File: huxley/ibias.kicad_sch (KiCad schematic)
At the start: 4 parts, among them U2 LM134H

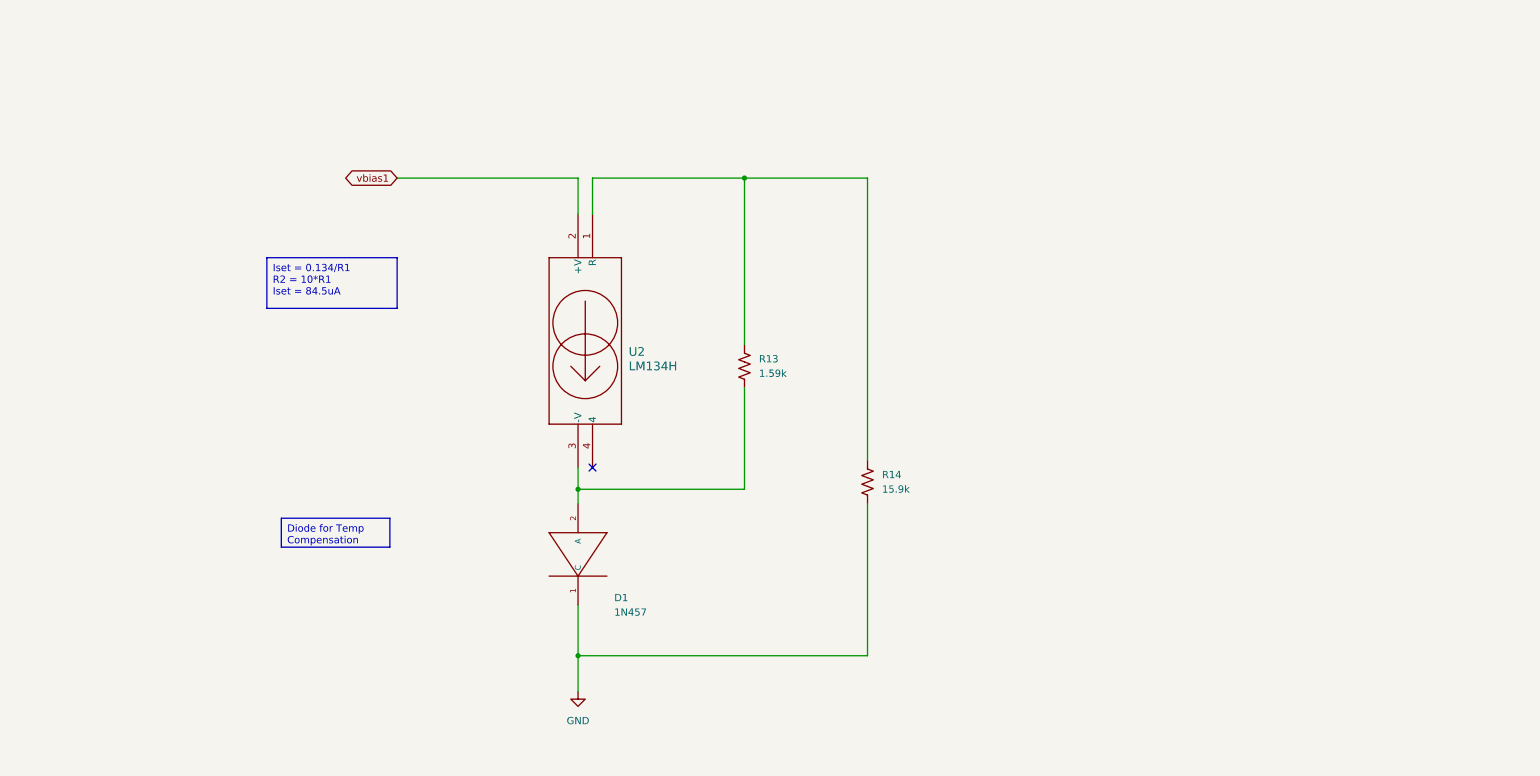
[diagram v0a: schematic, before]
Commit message: updated Ibias gen and footprints
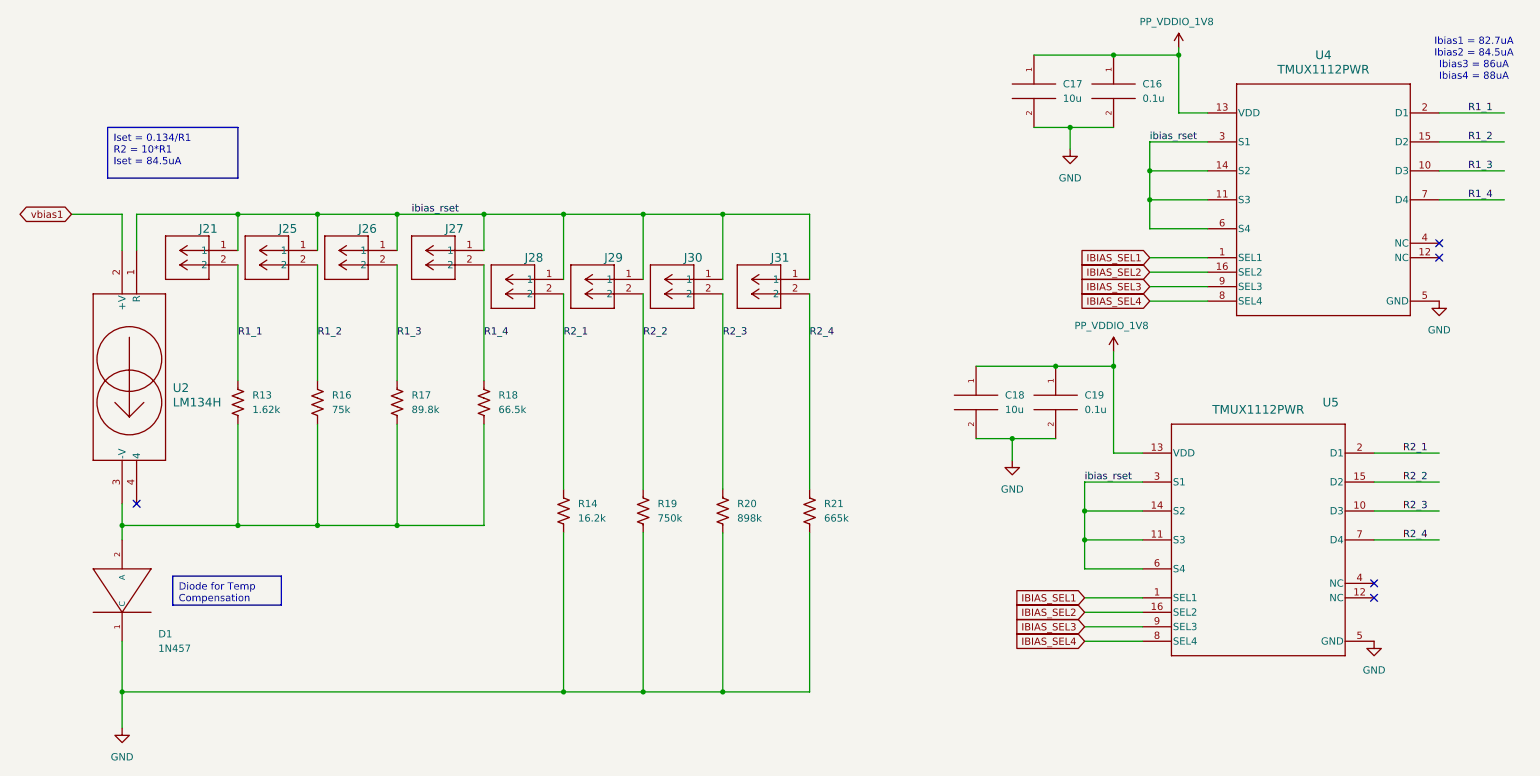
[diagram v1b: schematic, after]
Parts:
- added C16, C19: 0.1u, Capacitor_SMD:C_0402_1005Metric, symbol pspice:C
- added C17, C18: 10u, Capacitor_SMD:C_0402_1005Metric, symbol pspice:C
- added J21, J25, J26, J27, J28, J29, J30, J31: 61300211121, 726_footprints:CONN_61300211121_WRE, symbol _PHASE:61300211121
- added R16: 75k, Resistor_SMD:R_0603_1608Metric, symbol Device:R_US
- added R17: 89.8k, Resistor_SMD:R_0603_1608Metric, symbol Device:R_US
- added R18: 66.5k, Resistor_SMD:R_0603_1608Metric, symbol Device:R_US
- added R19: 750k, Resistor_SMD:R_0603_1608Metric, symbol Device:R_US
- added R20: 898k, Resistor_SMD:R_0603_1608Metric, symbol Device:R_US
- added R21: 665k, Resistor_SMD:R_0603_1608Metric, symbol Device:R_US
- added U4, U5: TMUX1112PWR, 726_footprints:TMUX1111PWR, symbol _PHASE:TMUX1111PWR
- R13: value 1.59k -> 1.62k
- R14: value 15.9k -> 16.2k
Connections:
- net GND: now also C16.2, C17.2, C18.2, C19.2, R19.2, R20.2, R21.2, U4.5 (GND), U5.5 (GND)
- net at D1.2 (A), R13.2, U2.3 (-V): now also R16.2, R17.2, R18.2
- new net IBIAS_SEL1: U4.1 (SEL1), U5.1 (SEL1)
- new net IBIAS_SEL2: U4.16 (SEL2), U5.16 (SEL2)
- new net IBIAS_SEL3: U4.9 (SEL3), U5.9 (SEL3)
- new net IBIAS_SEL4: U4.8 (SEL4), U5.8 (SEL4)
- new net PP_VDDIO_1V8: C16.1, C17.1, C18.1, C19.1, U4.13 (VDD), U5.13 (VDD)
- new net R1_1: J21.2, R13.1, U4.2 (D1)
- new net R1_2: J25.2, R16.1, U4.15 (D2)
- new net R1_3: J26.2, R17.1, U4.10 (D3)
- new net R1_4: J27.2, R18.1, U4.7 (D4)
- new net R2_1: J28.2, R14.1, U5.2 (D1)
- new net R2_2: J29.2, R19.1, U5.15 (D2)
- new net R2_3: J30.2, R20.1, U5.10 (D3)
- new net R2_4: J31.2, R21.1, U5.7 (D4)
- new net ibias_rset: J21.1, J25.1, J26.1, J27.1, J28.1, J29.1, J30.1, J31.1, U2.1 (R), U4.11 (S3), U4.14 (S2), U4.3 (S1), U4.6 (S4), U5.11 (S3), U5.14 (S2), U5.3 (S1), U5.6 (S4)
- no-connect marks 1 -> 5
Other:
- note added: "Ibias1 = 82.7uA Ibias2 = 84.5uA Ibias3 = 86uA Ibias4 = 88uA"
- moved on the sheet: D1, R13, R14, U2

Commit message: updated footprints
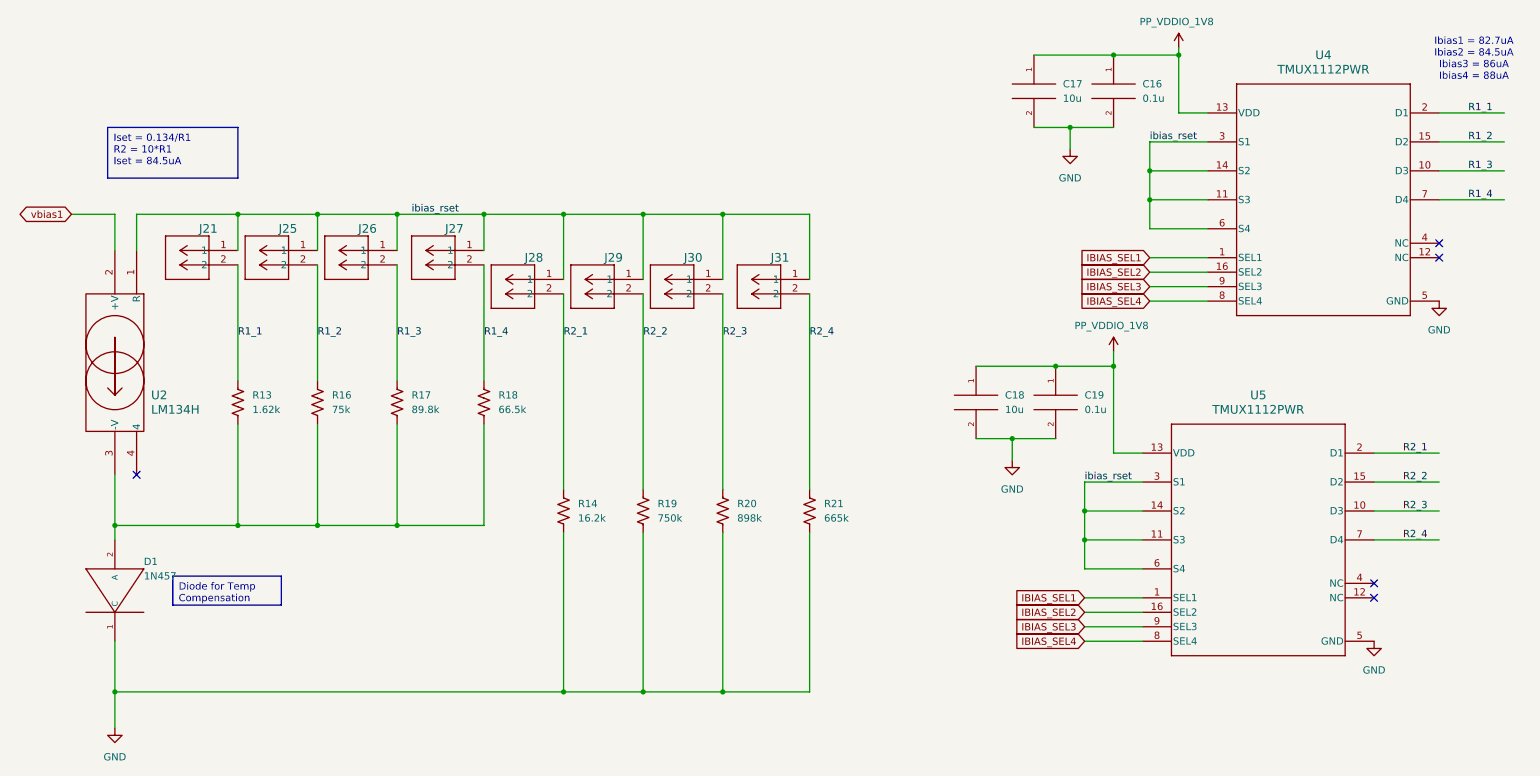
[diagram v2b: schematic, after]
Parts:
- removed U4, U5: TMUX1112PWR, 726_footprints:TMUX1111PWR, symbol _PHASE:TMUX1111PWR
- added U4, U5: TMUX1112PWR, 726_footprints:TMUX1111PWR, symbol _PHASE:TMUX1112PWR
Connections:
- net GND: now also U4.5 (GND), U5.5 (GND)
- net IBIAS_SEL1: now also U4.1 (SEL1), U5.1 (SEL1)
- net IBIAS_SEL2: now also U4.16 (SEL2), U5.16 (SEL2)
- net IBIAS_SEL3: now also U4.9 (SEL3), U5.9 (SEL3)
- net IBIAS_SEL4: now also U4.8 (SEL4), U5.8 (SEL4)
- net PP_VDDIO_1V8: now also U4.13 (VDD), U5.13 (VDD)
- net R1_1: now also U4.2 (D1)
- net R1_2: now also U4.15 (D2)
- net R1_3: now also U4.10 (D3)
- net R1_4: now also U4.7 (D4)
- net R2_1: now also U5.2 (D1)
- net R2_2: now also U5.15 (D2)
- net R2_3: now also U5.10 (D3)
- net R2_4: now also U5.7 (D4)
- net ibias_rset: now also U4.11 (S3), U4.14 (S2), U4.3 (S1), U4.6 (S4), U5.11 (S3), U5.14 (S2), U5.3 (S1), U5.6 (S4)
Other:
- moved on the sheet: D1

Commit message: layout
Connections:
- net PP_VDDIO_1V8 renamed PP_TAVDD_1V8
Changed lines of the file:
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@@
 			)
 		)
-		(property "Value" "PP_VDDIO_1V8"
+		(property "Value" "PP_TAVDD_1V8"
 			(at 203.962 69.088 0)
 			(effects
@@
 			)
 		)
-		(property "Value" "PP_VDDIO_1V8"
+		(property "Value" "PP_TAVDD_1V8"
 			(at 215.392 15.748 0)
 			(effects

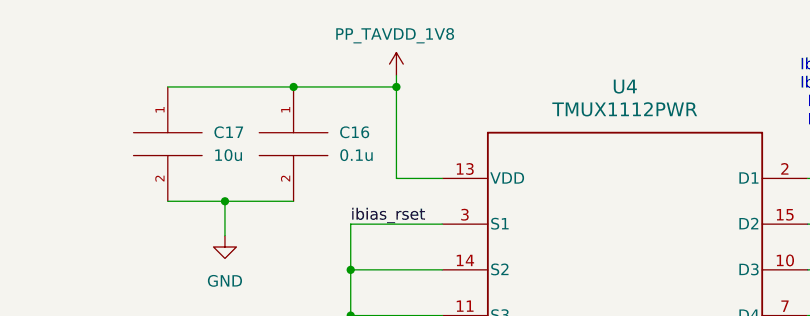
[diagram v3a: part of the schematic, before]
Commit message: added banana plugs and fixed analog discovery pinout
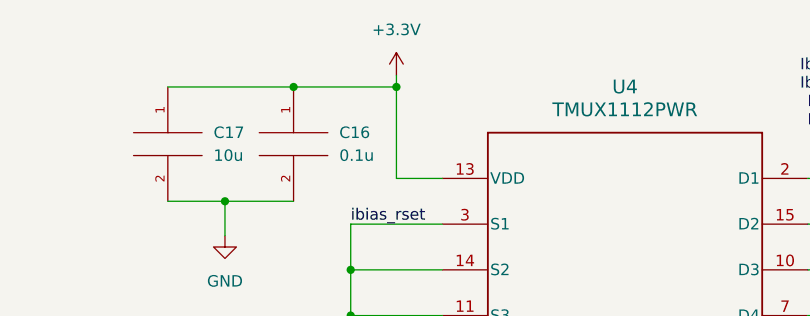
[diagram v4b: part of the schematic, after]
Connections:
- net PP_TAVDD_1V8: no longer C16.1, C17.1, U4.13 (VDD)
- new net +3.3V: C16.1, C17.1, U4.13 (VDD)
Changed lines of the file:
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@@
+	)
+	(symbol
+		(lib_id "power:+3.3V")
+		(at 222.25 20.32 0)
+		(unit 1)
+		(exclude_from_sim no)
+		(in_bom yes)
+		(on_board yes)
+		(dnp no)
+		(fields_autoplaced yes)
+		(property "Reference" "#PWR03"
+			(at 222.25 24.13 0)
+			(effects
+				(font
+					(size 1.27 1.27)
+				)
+				(hide yes)
+			)
+		)
+		(property "Value" "+3.3V"
+			(at 222.25 15.24 0)
+			(effects
+				(font
+					(size 1.27 1.27)
+				)
+			)
+		)
+		(property "Footprint" ""
+			(at 222.25 20.32 0)
+			(effects
+				(font
+					(size 1.27 1.27)
+				)
+				(hide yes)
+			)
+		)
+		(property "Datasheet" ""
+			(at 222.25 20.32 0)
+			(effects
+				(font
+					(size 1.27 1.27)
+				)
+				(hide yes)
+			)
+		)
+		(property "Description" "Power symbol creates a global label with name \"+3.3V\""
+			(at 222.25 20.32 0)
+			(effects
+				(font
+					(size 1.27 1.27)
+				)
+				(hide yes)
+			)
+		)
+		(pin "1"
+		)
+		(instances
+			(project "huxley"
+				(path "/c6103430-c27a-4e90-8e2e-9404255f5ee3/b75e3563-89bb-4794-9213-b0fc22374a5c"
+					(reference "#PWR03")
+					(unit 1)
+				)
+			)
+		)
 	)
 	(symbol
@@
 					(unit 1)
 				)
-			)
-		)
-	)
-	(symbol
-		(lib_id "power:+1V8")
-		(at 222.25 20.32 0)
-		(unit 1)
-		(exclude_from_sim no)
-		(in_bom yes)
-		(on_board yes)
-		(dnp no)
-		(property "Reference" "#PWR03"
-			(at 222.25 24.13 0)
-			(effects
-				(font
-					(size 1.27 1.27)
-				)
-				(hide yes)
-			)
-		)
-		(property "Value" "PP_TAVDD_1V8"
-			(at 215.392 15.748 0)
-			(effects
-				(font
-					(size 1.27 1.27)
-				)
-				(justify left)
-			)
-		)
-		(property "Footprint" ""
-			(at 222.25 20.32 0)
-			(effects
-				(font
-					(size 1.27 1.27)
-				)
-				(hide yes)
-			)
-		)
-		(property "Datasheet" ""
-			(at 222.25 20.32 0)
-			(effects
-				(font
-					(size 1.27 1.27)
-				)
-				(hide yes)
-			)
-		)
-		(property "Description" "Power symbol creates a global label with name \"+1V8\""
-			(at 222.25 20.32 0)
-			(effects
-				(font
-					(size 1.27 1.27)
-				)
-				(hide yes)
-			)
-		)
-		(pin "1"
-		)
-		(instances
-			(project "huxley"
-				(path "/c6103430-c27a-4e90-8e2e-9404255f5ee3/b75e3563-89bb-4794-9213-b0fc22374a5c"
-					(reference "#PWR03")
-					(unit 1)
-				)

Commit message: layout_1003
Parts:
- C16, C17, C18, C19: footprint Capacitor_SMD:C_0402_1005Metric -> Capacitor_SMD:C_0603_1608Metric
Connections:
- net PP_TAVDD_1V8 is gone; now on net +3.3V: C18.1, C19.1, U5.13 (VDD)
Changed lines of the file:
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@@
 			)
 		)
-		(property "Footprint" "Capacitor_SMD:C_0402_1005Metric"
+		(property "Footprint" "Capacitor_SMD:C_0603_1608Metric"
 			(at 200.66 82.55 0)
 			(effects
@@
 			)
 		)
-		(property "Footprint" "Capacitor_SMD:C_0402_1005Metric"
+		(property "Footprint" "Capacitor_SMD:C_0603_1608Metric"
 			(at 196.85 27.94 0)
 			(effects
@@
 			)
 		)
-		(property "Footprint" "Capacitor_SMD:C_0402_1005Metric"
+		(property "Footprint" "Capacitor_SMD:C_0603_1608Metric"
 			(at 186.69 82.55 0)
 			(effects
@@
 			)
 		)
-		(property "Footprint" "Capacitor_SMD:C_0402_1005Metric"
+		(property "Footprint" "Capacitor_SMD:C_0603_1608Metric"
 			(at 210.82 27.94 0)
 			(effects
@@
 			)
 		)
-		(property "Value" "PP_TAVDD_1V8"
+		(property "Value" "+3.3V"
 			(at 203.962 69.088 0)
 			(effects

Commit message: layout_1003_1
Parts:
- U4, U5: footprint 726_footprints:TMUX1111PWR -> Package_SO:TSSOP-16_4.4x5mm_P0.65mm
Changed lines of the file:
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@@
 			)
 		)
-		(property "Footprint" "726_footprints:TMUX1111PWR"
+		(property "Footprint" "Package_SO:TSSOP-16_4.4x5mm_P0.65mm"
 			(at 236.22 106.68 0)
 			(effects
@@
 			)
 		)
-		(property "Footprint" "726_footprints:TMUX1111PWR"
+		(property "Footprint" "Package_SO:TSSOP-16_4.4x5mm_P0.65mm"
 			(at 247.65 46.99 0)
 			(effects

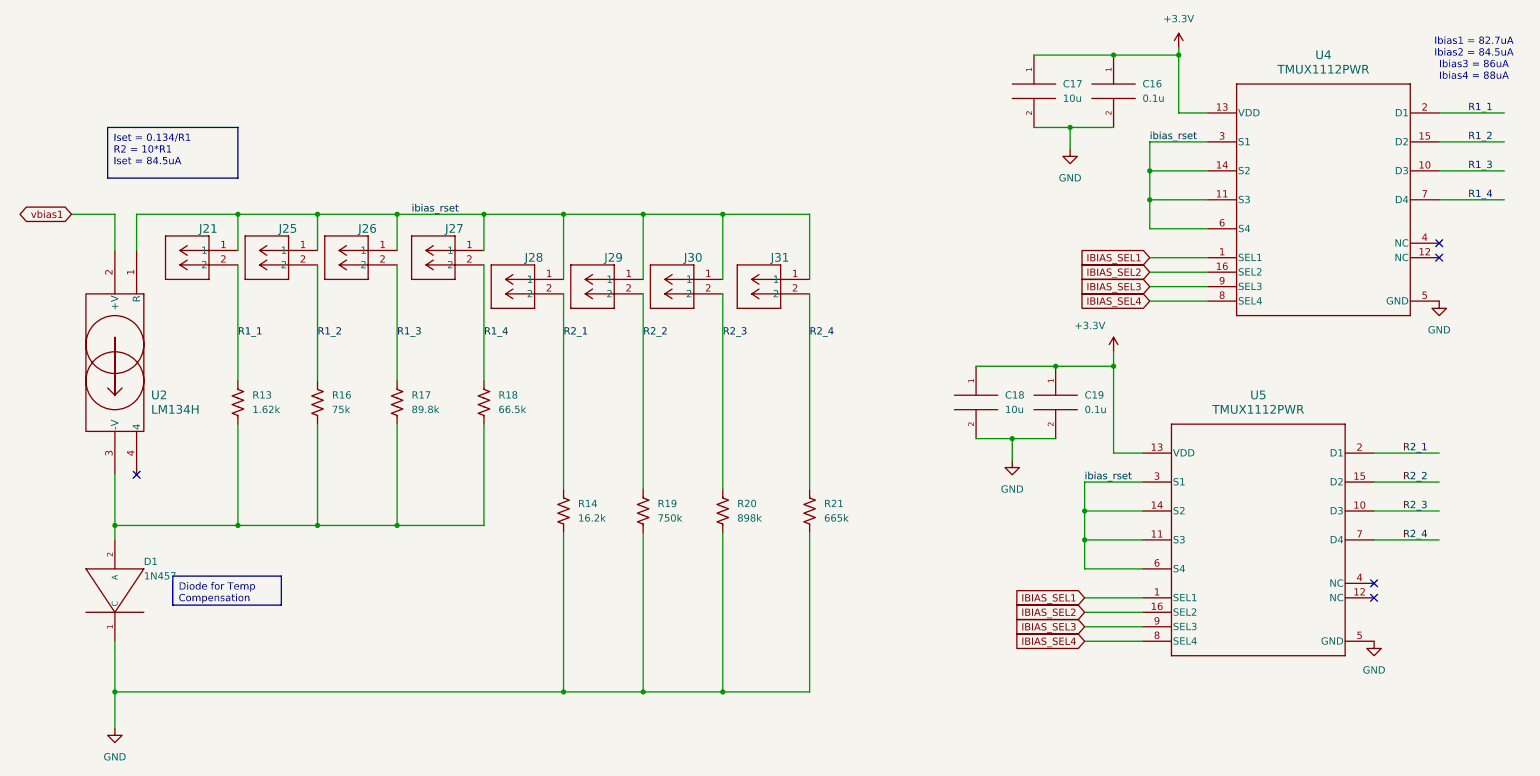
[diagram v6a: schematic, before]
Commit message: reorganized pin assignment to level shifter; matched 3V3 power net name; minor schematic cleanup
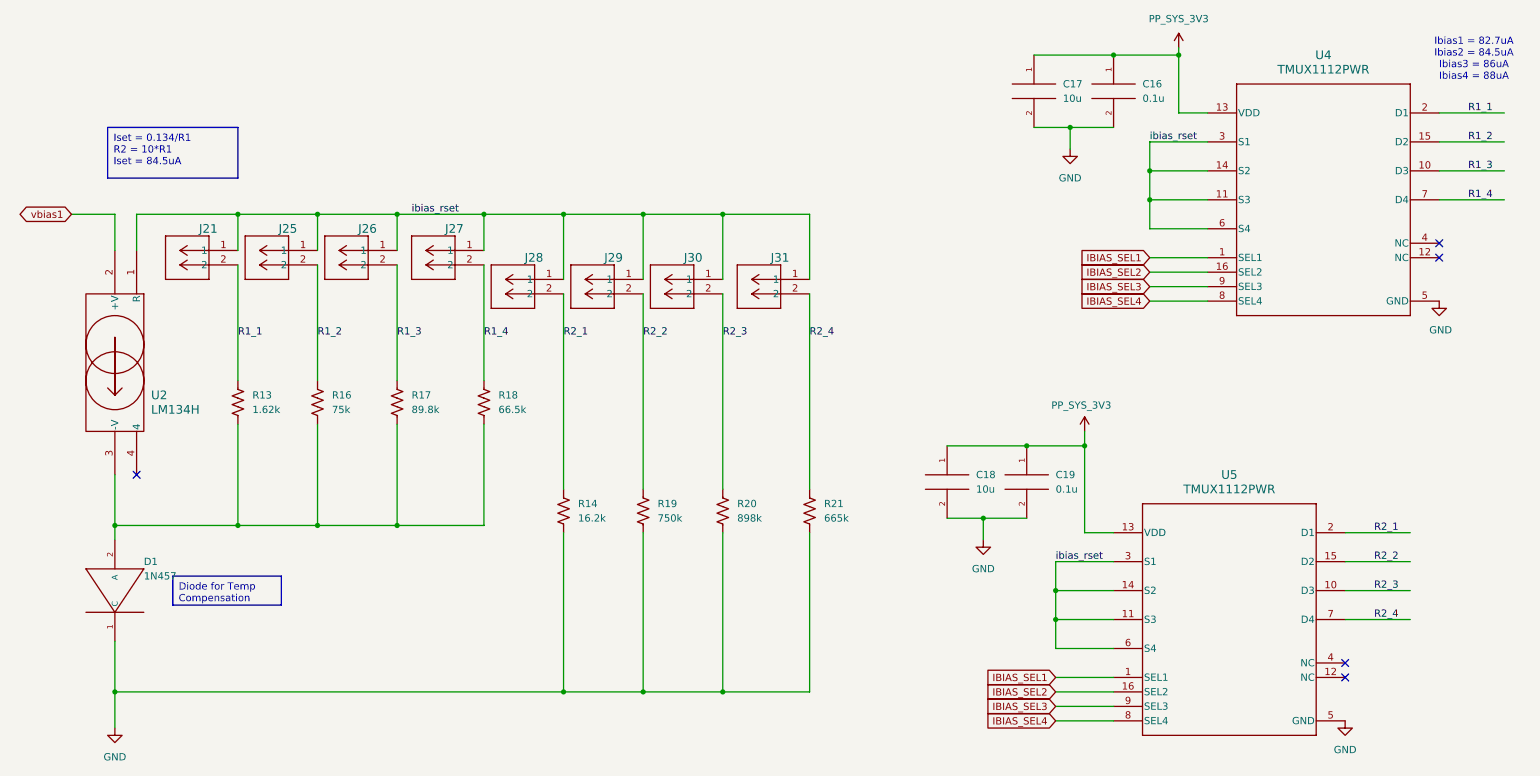
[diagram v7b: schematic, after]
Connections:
- net +3.3V renamed PP_SYS_3V3
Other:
- moved on the sheet: C18, C19, U5
